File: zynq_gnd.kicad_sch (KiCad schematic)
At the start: 1 part, among them U1 XC7Z007S-1CLG225C

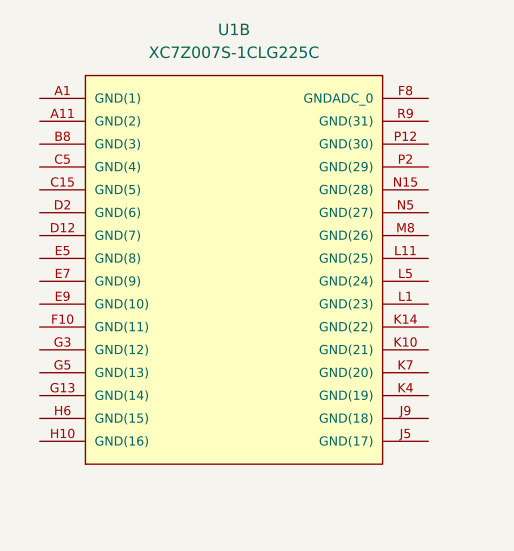
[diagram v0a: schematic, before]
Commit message: update zynq_gnd page
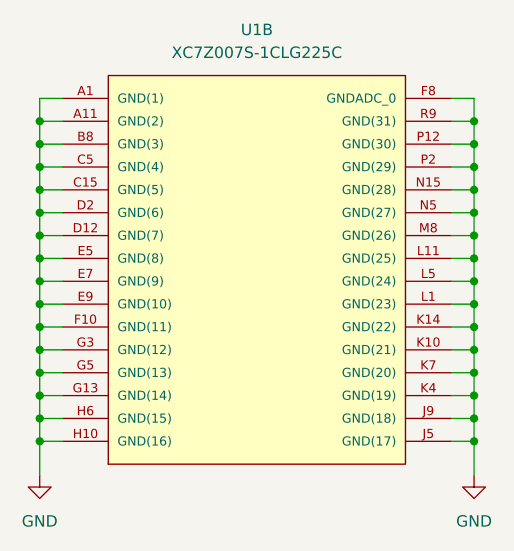
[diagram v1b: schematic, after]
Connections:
- net GND: now reaches U1.A1 (GND(1))
- net GND: now also U1.A11 (GND(2)), U1.B8 (GND(3)), U1.C15 (GND(5)), U1.C5 (GND(4)), U1.D12 (GND(7)), U1.D2 (GND(6)), U1.E5 (GND(8)), U1.E7 (GND(9)), U1.E9 (GND(10)), U1.F10 (GND(11)), U1.F8 (GNDADC_0), U1.G13 (GND(14)), U1.G3 (GND(12)), U1.G5 (GND(13)), U1.H10 (GND(16)), U1.H6 (GND(15)), U1.J5 (GND(17)), U1.J9 (GND(18)), U1.K10 (GND(21)), U1.K14 (GND(22)), U1.K4 (GND(19)), U1.K7 (GND(20)), U1.L1 (GND(23)), U1.L11 (GND(25)), U1.L5 (GND(24)), U1.M8 (GND(26)), U1.N15 (GND(28)), U1.N5 (GND(27)), U1.P12 (GND(30)), U1.P2 (GND(29)), U1.R9 (GND(31))
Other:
- moved on the sheet: U1B
